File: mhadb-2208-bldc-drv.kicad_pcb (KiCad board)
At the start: 2 copper layers, 0 parts

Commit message: pcb: import components from schema
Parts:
- added C1: 22u, Capacitor_SMD:C_1206_3216Metric, F.Cu at (96.0, 159.1)
- added C10: 0u1, Capacitor_SMD:C_0402_1005Metric, F.Cu at (91.3, 148.8)
- added C11: 0u1, Capacitor_SMD:C_0402_1005Metric, F.Cu at (91.3, 150.7)
- added C12: 1u, Capacitor_SMD:C_0402_1005Metric, F.Cu at (91.3, 152.7)
- added C13: 1u, Capacitor_SMD:C_0402_1005Metric, F.Cu at (91.3, 154.7)
- added C14: 10n, Capacitor_SMD:C_0402_1005Metric, F.Cu at (94.2, 148.8)
- added C15: 22u, Capacitor_SMD:C_1206_3216Metric, F.Cu at (96.0, 165.8)
- added C2: 22u, Capacitor_SMD:C_1206_3216Metric, F.Cu at (96.0, 162.5)
- added C3: 0u1, Capacitor_SMD:C_0402_1005Metric, F.Cu at (88.4, 148.8)
- added C32: 1u, Capacitor_SMD:C_0402_1005Metric, F.Cu at (94.2, 150.7)
- added C35: 1u, Capacitor_SMD:C_0402_1005Metric, F.Cu at (94.2, 152.7)
- added C36: 10n, Capacitor_SMD:C_0402_1005Metric, F.Cu at (94.2, 154.7)
- added C37: 0u1, Capacitor_SMD:C_0402_1005Metric, F.Cu at (97.0, 148.8)
- added C38: 0u1, Capacitor_SMD:C_0402_1005Metric, F.Cu at (97.0, 150.7)
- added C39: 10u, Capacitor_SMD:C_0805_2012Metric, F.Cu at (84.8, 141.0)
- added C4: 10u, Capacitor_SMD:C_0805_2012Metric, F.Cu at (84.8, 137.9)
- added C40: 0u1, Capacitor_SMD:C_0402_1005Metric, F.Cu at (97.0, 152.7)
- added C41: 1u, Capacitor_SMD:C_0402_1005Metric, F.Cu at (97.0, 154.7)
- added C42: 100u, Capacitor_SMD:CP_Elec_6.3x7.7, F.Cu at (83.3, 161.5)
- added C43: 10u, Capacitor_SMD:C_0805_2012Metric, F.Cu at (84.8, 144.0)
- added C5: 0u1, Capacitor_SMD:C_0402_1005Metric, F.Cu at (88.4, 150.7)
- added C6: 20p, Capacitor_SMD:C_0603_1608Metric, F.Cu at (80.1, 166.8)
- added C7: 20p, Capacitor_SMD:C_0603_1608Metric, F.Cu at (80.1, 169.4)
- added C8: 0u1, Capacitor_SMD:C_0402_1005Metric, F.Cu at (88.4, 152.7)
- added C9: 0u1, Capacitor_SMD:C_0402_1005Metric, F.Cu at (88.4, 154.7)
- added D10: H5VU10U, GLCS:Diode_DFN1006, F.Cu at (76.7, 172.4)
- added D11: YELLOW, LED_SMD:LED_0805_2012Metric, F.Cu at (90.8, 171.2)
- added D3: H5VU10U, GLCS:Diode_DFN1006, F.Cu at (76.7, 158.4)
- added D4: H5VU10U, GLCS:Diode_DFN1006, F.Cu at (76.7, 160.4)
- added D5: H5VU10U, GLCS:Diode_DFN1006, F.Cu at (76.7, 162.4)
- added D6: H5VU10U, GLCS:Diode_DFN1006, F.Cu at (76.7, 164.4)
- added D7: H5VU10U, GLCS:Diode_DFN1006, F.Cu at (76.7, 166.4)
- added D8: H5VU10U, GLCS:Diode_DFN1006, F.Cu at (76.7, 168.4)
- added D9: H5VU10U, GLCS:Diode_DFN1006, F.Cu at (76.7, 170.4)
- added FB1: 600Ω@100M, Inductor_SMD:L_0805_2012Metric, F.Cu at (84.4, 167.0)
- added FB2: 600Ω@100M, Inductor_SMD:L_0805_2012Metric, F.Cu at (84.4, 169.7)
- added J1: TC2030, Connector:Tag-Connect_TC2030-IDC-NL_2x03_P1.27mm_Vertical, F.Cu at (91.0, 139.0)
- added J2: Conn_01x04_Pin, Connector_PinHeader_2.54mm:PinHeader_1x04_P2.54mm_Vertical, F.Cu at (90.8, 159.7)
- added J3: Conn_01x04, Connector_JST:JST_PH_S4B-PH-K_1x04_P2.00mm_Horizontal, F.Cu at (78.0, 150.2)
- added JP1: Jumper_2_Small_Bridged, Jumper:SolderJumper-2_P1.3mm_Open_RoundedPad1.0x1.5mm, F.Cu at (96.5, 143.3)
- added M2: Motor_3_Phases, Connector_PinHeader_2.54mm:PinHeader_1x03_P2.54mm_Vertical, F.Cu at (80.2, 138.7)
- added R1: 10k, Resistor_SMD:R_0402_1005Metric, F.Cu at (64.0, 157.7)
- added R2: 10k, Resistor_SMD:R_0402_1005Metric, F.Cu at (64.0, 159.7)
- added R29: 10k, Resistor_SMD:R_0402_1005Metric, F.Cu at (64.0, 165.6)
- added R3: 120, Resistor_SMD:R_1206_3216Metric, F.Cu at (69.4, 171.7)
- added R4: 10k, Resistor_SMD:R_0402_1005Metric, F.Cu at (64.0, 161.7)
- added R5: 560, Resistor_SMD:R_0603_1608Metric, F.Cu at (80.1, 171.9)
- added R6: 5k1, Resistor_SMD:R_0402_1005Metric, F.Cu at (64.0, 163.7)
- added SW1: SW_Push, Button_Switch_SMD:SW_SPST_TS-1088-xR020, F.Cu at (70.1, 163.2)
- added SW4: SW_Push, Button_Switch_SMD:SW_SPST_TS-1088-xR020, F.Cu at (70.1, 167.8)
- added TP3: TestPoint, TestPoint:TestPoint_Pad_D2.0mm, F.Cu at (64.6, 138.5)
- added TP5: TestPoint, TestPoint:TestPoint_Pad_D2.0mm, F.Cu at (64.6, 142.5)
- added TP6: TestPoint, TestPoint:TestPoint_Pad_D2.0mm, F.Cu at (64.6, 146.6)
- added TP8: TestPoint, TestPoint:TestPoint_Pad_D2.0mm, F.Cu at (64.6, 150.6)
- added TP9: TestPoint, TestPoint:TestPoint_Pad_D2.0mm, F.Cu at (64.6, 154.7)
- added U1: AS5600-ASOT, Package_SO:SOIC-8_3.9x4.9mm_P1.27mm, F.Cu at (70.8, 151.2)
- added U10: DRV8311H, GLCS:Texas_RRW0024A_WQFN-24-1EP_2x2mm_P0.4mmThermalVias, F.Cu at (96.0, 169.8)
- added U2: SN65HVD230, Package_SO:SOIC-8_3.9x4.9mm_P1.27mm, F.Cu at (70.8, 157.7)
- added U3: STM32F103C8Tx, Package_QFP:LQFP-48_7x7mm_P0.5mm, F.Cu at (72.3, 142.1)
- added Y1: 8M, Crystal:Crystal_SMD_5032-2Pin_5.0x3.2mm, F.Cu at (90.7, 144.1)

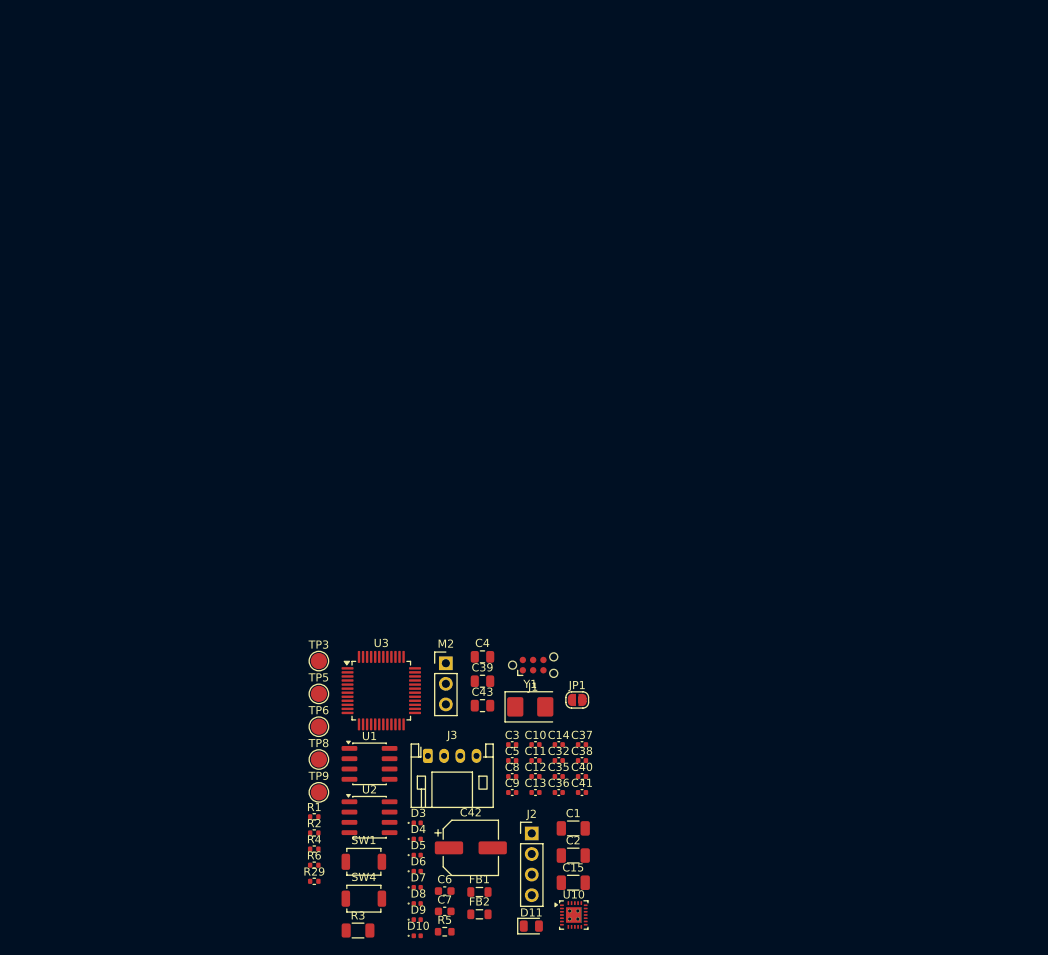
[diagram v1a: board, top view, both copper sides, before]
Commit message: schem/pcb: add motor mounting holes
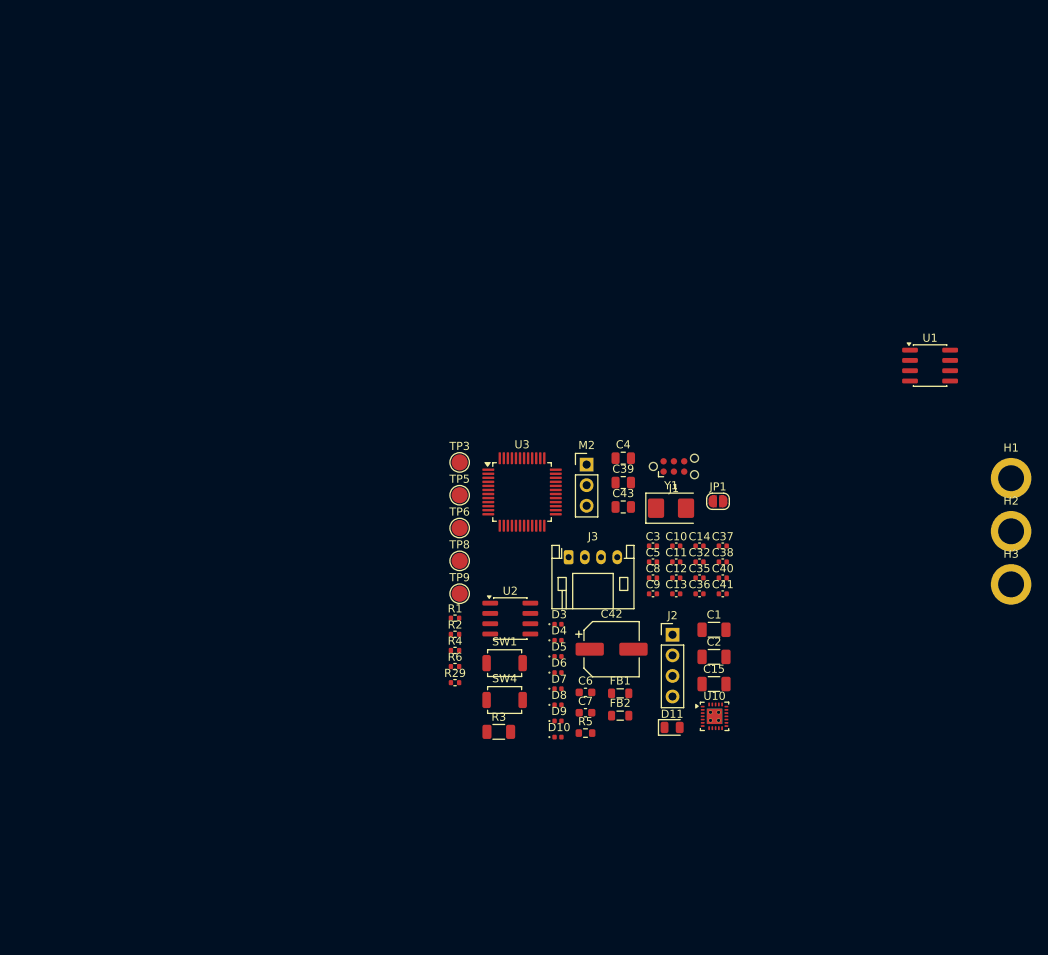
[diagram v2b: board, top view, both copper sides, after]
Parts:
- added H1: MountingHole_Pad, GLCS:MountingHole_3.2mm_M3_DIN965_Pad_Thin, F.Cu at (150.0, 115.9)
- added H2: MountingHole_Pad, GLCS:MountingHole_3.2mm_M3_DIN965_Pad_Thin, F.Cu at (150.0, 122.5)
- added H3: MountingHole_Pad, GLCS:MountingHole_3.2mm_M3_DIN965_Pad_Thin, F.Cu at (150.0, 129.0)
- moved U1 84.9 mm to (140.0, 102.0)
- moved C1 30.0 mm to (113.3, 134.6)
- moved C12 30.0 mm to (108.7, 128.2)
- moved C13 30.0 mm to (108.7, 130.2)
- moved C2 30.0 mm to (113.3, 137.9)
- moved C39 30.0 mm to (102.1, 116.4)
- moved C40 30.0 mm to (114.4, 128.2)
- moved C41 30.0 mm to (114.4, 130.2)
- moved C8 30.0 mm to (105.8, 128.2)
- moved C9 30.0 mm to (105.8, 130.2)
- moved FB1 30.0 mm to (101.8, 142.4)
- moved FB2 30.0 mm to (101.8, 145.2)
- moved J2 30.0 mm to (108.2, 135.2)
- moved M2 30.0 mm to (97.6, 114.2)
- moved R3 30.0 mm to (86.8, 147.2)
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
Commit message: pcb: add edge cut
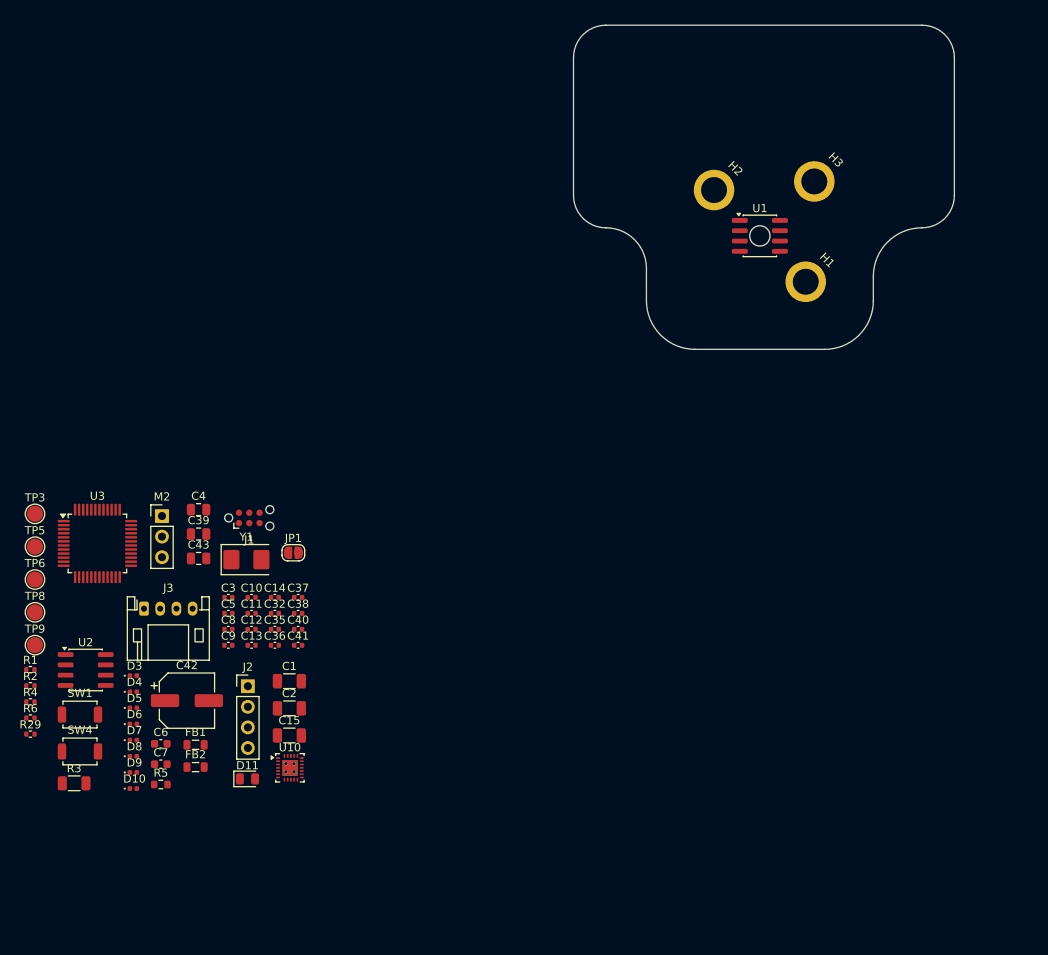
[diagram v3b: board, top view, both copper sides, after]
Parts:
- moved H2 55.8 mm to (113.3, 80.3), turned to -45 degrees
- moved H3 55.3 mm to (125.7, 79.3), turned to -45 degrees
- moved C1 52.8 mm to (60.9, 140.9)
- moved C10 52.8 mm to (56.3, 130.6)
- moved C11 52.8 mm to (56.3, 132.6)
- moved C12 52.8 mm to (56.3, 134.6)
- moved C13 52.8 mm to (56.3, 136.5)
- moved C15 52.8 mm to (60.9, 147.7)
- moved C2 52.8 mm to (60.9, 144.3)
- moved C3 52.8 mm to (53.4, 130.6)
- moved C42 52.8 mm to (48.3, 143.3)
- moved C5 52.8 mm to (53.4, 132.6)
- moved C6 52.8 mm to (45.1, 148.7)
- moved C7 52.8 mm to (45.1, 151.2)
- moved C8 52.8 mm to (53.4, 134.6)
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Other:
- board outline added: 47 x 40 mm

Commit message: schem/pcb: fix DRV8311 nsleep
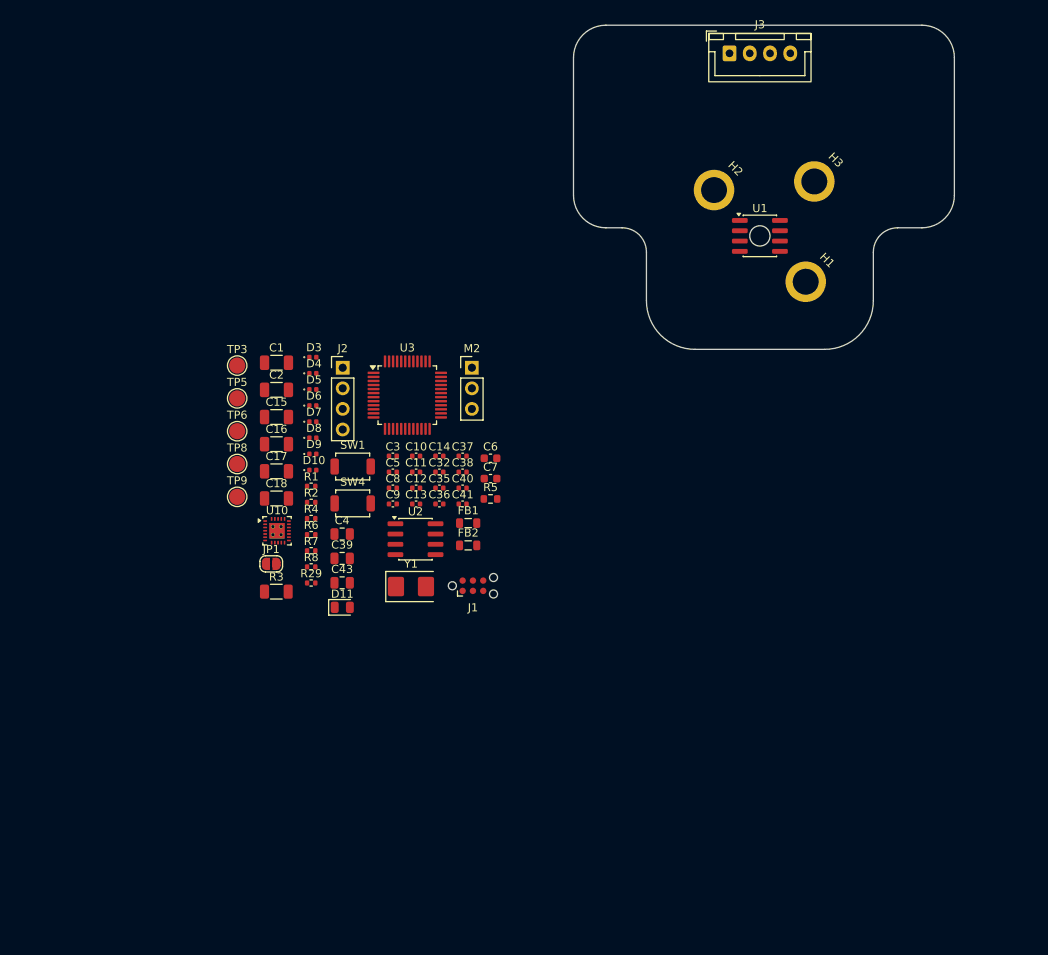
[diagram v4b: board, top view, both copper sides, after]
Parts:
- removed C42: 100u, Capacitor_SMD:CP_Elec_6.3x7.7
- added C16: 22u, Capacitor_SMD:C_1206_3216Metric, F.Cu at (59.4, 111.7)
- added C17: 22u, Capacitor_SMD:C_1206_3216Metric, F.Cu at (59.4, 115.0)
- added C18: 22u, Capacitor_SMD:C_1206_3216Metric, F.Cu at (59.4, 118.4)
- added R7: 10k, Resistor_SMD:R_0402_1005Metric, F.Cu at (63.6, 124.8)
- added R8: 5k1, Resistor_SMD:R_0402_1005Metric, F.Cu at (63.6, 126.8)
- J3: footprint Connector_JST:JST_PH_S4B-PH-K_1x04_P2.00mm_Horizontal -> Connector_JST:JST_XH_B4B-XH-A_1x04_P2.50mm_Vertical
- moved J3 99.6 mm to (115.2, 63.5)
- moved C6 53.8 mm to (85.8, 113.4)
- moved C7 53.8 mm to (85.8, 116.0)
- moved R5 53.8 mm to (85.8, 118.5)
- moved SW1 45.5 mm to (68.8, 114.5)
- moved SW4 45.5 mm to (68.8, 119.0)
- moved D3 45.1 mm to (63.8, 101.0)
- moved D6 45.1 mm to (63.8, 106.9)
- moved D9 45.1 mm to (63.8, 112.9)
- moved D4 45.1 mm to (63.8, 103.0)
- moved D5 45.1 mm to (63.8, 105.0)
- moved D8 45.1 mm to (63.8, 110.9)
- moved D10 45.1 mm to (63.8, 114.9)
- moved D7 45.1 mm to (63.8, 108.9)
- moved U2 43.8 mm to (76.5, 123.4)
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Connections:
- U10 pad 24: +5V -> Net-(U10-~{SLEEP})
- U3 pad 20: unconnected-(U3-PB2-Pad20) -> GND
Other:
- outline, holes or cut-outs redrawn

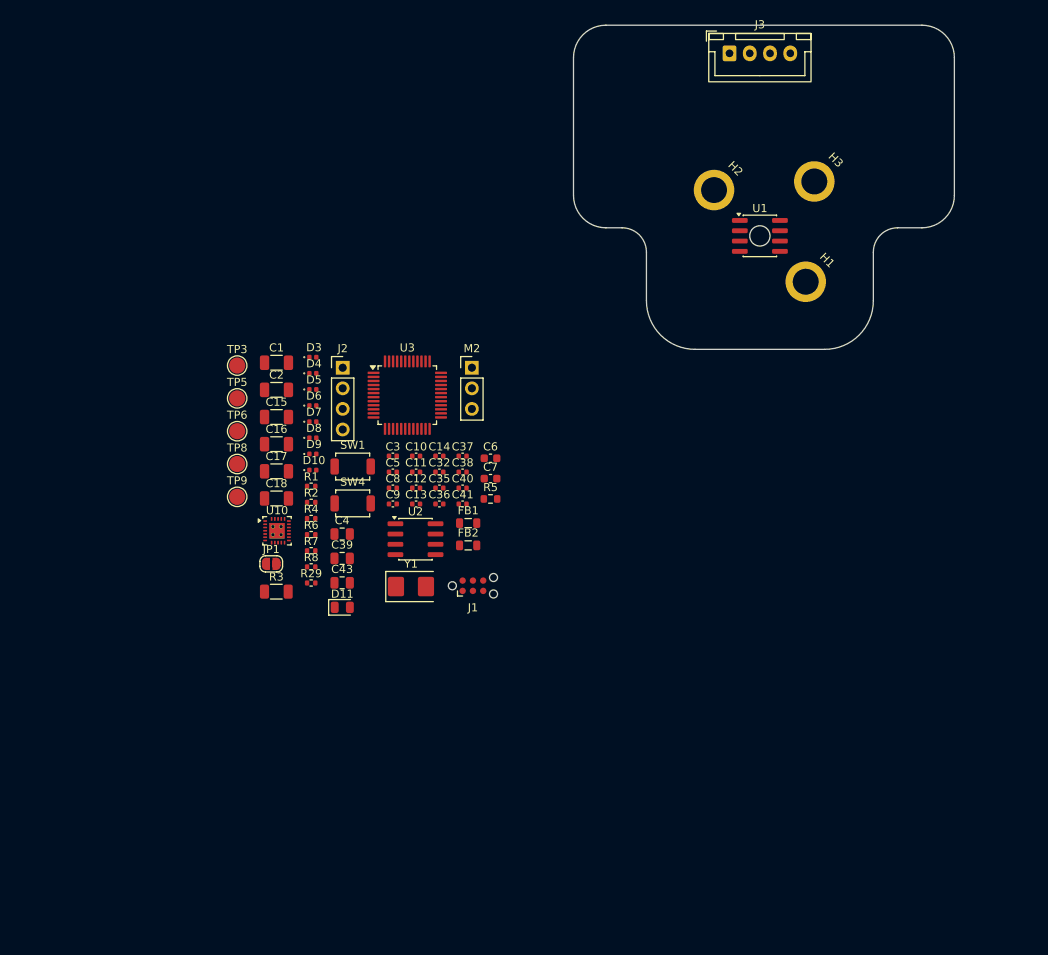
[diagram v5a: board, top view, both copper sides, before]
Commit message: pcb: initial rough placement
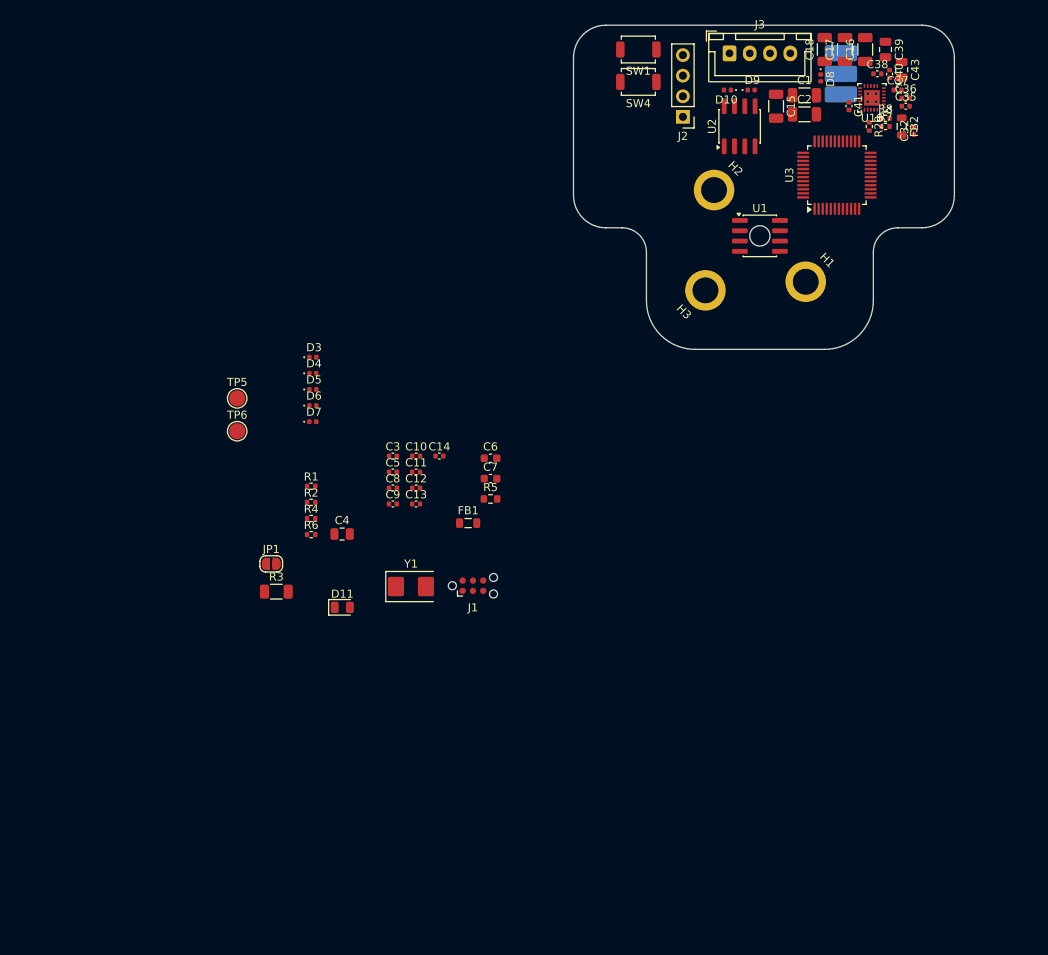
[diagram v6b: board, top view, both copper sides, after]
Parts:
- removed TP3, TP8, TP9: TestPoint, TestPoint:TestPoint_Pad_D2.0mm
- M2: footprint Connector_PinHeader_2.54mm:PinHeader_1x03_P2.54mm_Vertical -> GLCS:Connector_Pad_1x03; moved to B.Cu
- moved C43 93.7 mm to (136.5, 65.5), turned to -90 degrees
- moved C39 91.9 mm to (134.5, 63.0), turned to -90 degrees
- moved U10 90.8 mm to (132.8, 69.0), turned to 180 degrees
- moved R8 89.9 mm to (134.5, 71.5)
- moved R29 89.0 mm to (132.5, 72.5), turned to -90 degrees
- moved R7 88.1 mm to (134.5, 72.5)
- moved C16 87.5 mm to (132.0, 63.0), turned to 90 degrees
- moved C18 87.4 mm to (127.0, 63.0), turned to 90 degrees
- moved C17 87.4 mm to (129.5, 63.0), turned to 90 degrees
- moved D8 76.8 mm to (126.5, 66.5), turned to -90 degrees
- moved C36 76.3 mm to (137.0, 69.0)
- moved FB2 74.4 mm to (136.5, 72.5), turned to -90 degrees
- moved C35 74.4 mm to (137.0, 70.0)
- moved C2 73.5 mm to (124.5, 71.0)
- moved C40 73.4 mm to (135.0, 66.0), turned to -90 degrees
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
